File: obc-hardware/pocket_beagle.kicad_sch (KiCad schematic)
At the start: 18 parts, among them U101 PocketBeagle

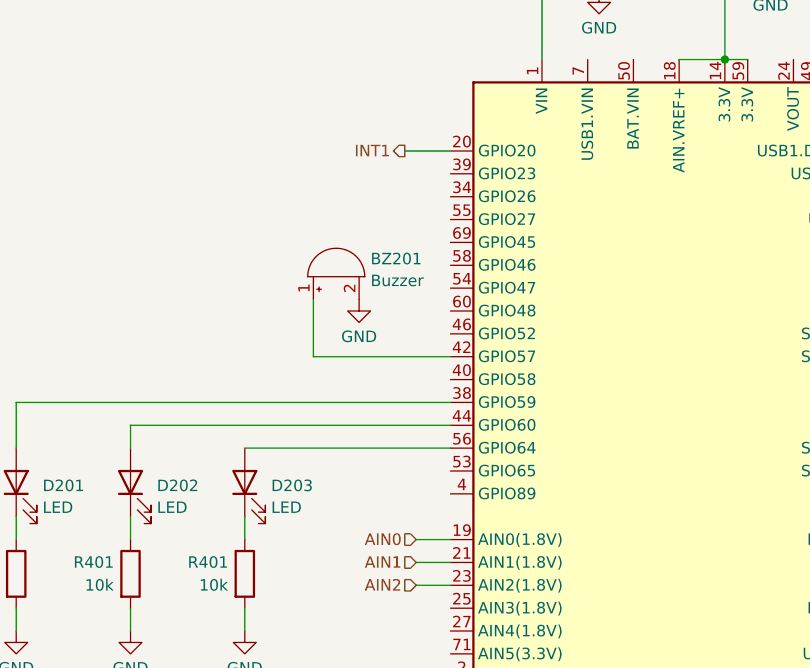
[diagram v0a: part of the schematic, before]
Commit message: added GPIO for payload
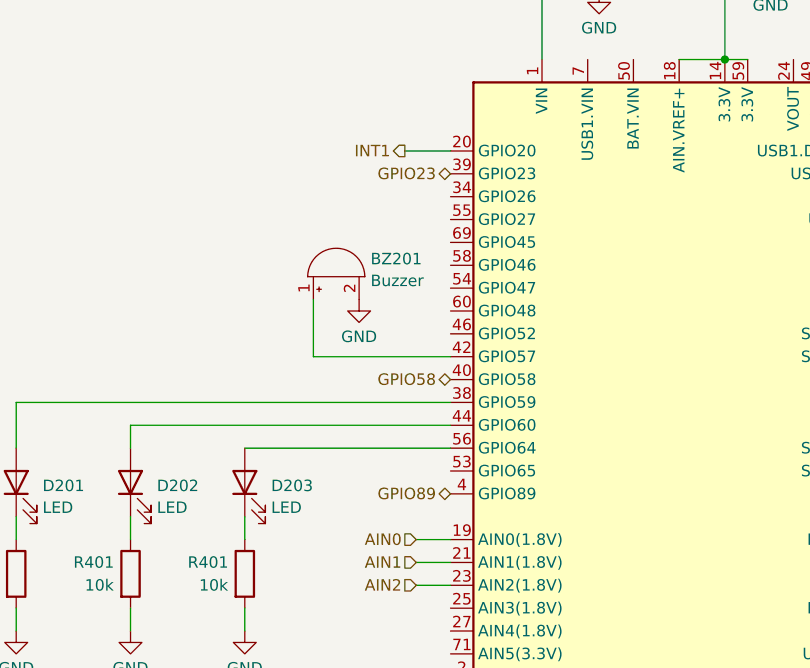
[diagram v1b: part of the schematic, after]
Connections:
- net GPIO23: now reaches U101.39 (GPIO23)
- net GPIO89: now reaches U101.4 (GPIO89)
- net GPIO58: now reaches U101.40 (GPIO58)
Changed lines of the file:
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@@
+    (effects (font (size 1.27 1.27)) (justify right))
+  )
+  (hierarchical_label "GPIO89" (shape bidirectional) (at 111.76 87.63 180) (fields_autoplaced)
+    (effects (font (size 1.27 1.27)) (justify right))
+  )
+  (hierarchical_label "GPIO58" (shape bidirectional) (at 111.76 74.93 180) (fields_autoplaced)
     (effects (font (size 1.27 1.27)) (justify right))
   )
@@
     (effects (font (size 1.27 1.27)) (justify right))
   )
+  (hierarchical_label "GPIO23" (shape bidirectional) (at 111.76 52.07 180) (fields_autoplaced)
+    (effects (font (size 1.27 1.27)) (justify right))
+  )

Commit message: added test points
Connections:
- net VOUT-24: now reaches U101.24 (VOUT)
- net AIN3: now reaches U101.25 (AIN3(1.8V))
- net AIN4: now reaches U101.27 (AIN4(1.8V))
- net PRU0.1: now reaches U101.33 (PRU0.1)
- net GPIO26: now reaches U101.34 (GPIO26)
- net PWM0A: now reaches U101.36 (PWM0A)
- net VOUT-49: now reaches U101.49 (VOUT)
- net BAT.VIN: now reaches U101.50 (BAT.VIN)
- net GPIO27: now reaches U101.55 (GPIO27)
- net PRU0.2: now reaches U101.68 (PRU0.2)
- net GPIO45: now reaches U101.69 (GPIO45)
- net AIN5: now reaches U101.71 (AIN5(3.3V))
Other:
- moved on the sheet: BZ201
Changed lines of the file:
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@@
+    (stroke (width 0) (type default))
+  )
+  (wire (pts (xy 166.37 120.65) (xy 162.56 120.65))
     (stroke (width 0) (type default))
   )
@@
     (stroke (width 0) (type default))
   )
-  (wire (pts (xy 96.52 72.39) (xy 96.52 66.04))
+  (wire (pts (xy 82.55 72.39) (xy 82.55 66.04))
     (stroke (width 0) (type default))
   )
@@
     (stroke (width 0) (type default))
   )
+  (wire (pts (xy 109.22 118.11) (xy 111.76 118.11))
+    (stroke (width 0) (type default))
+  )
   (wire (pts (xy 191.77 20.32) (xy 191.77 21.59))
     (stroke (width 0) (type default))
@@
     (stroke (width 0) (type default))
   )
+  (wire (pts (xy 149.86 36.83) (xy 149.86 39.37))
+    (stroke (width 0) (type default))
+  )
   (wire (pts (xy 76.2 100.33) (xy 76.2 102.87))
     (stroke (width 0) (type default))
@@
     (stroke (width 0) (type default))
   )
+  (wire (pts (xy 106.68 57.15) (xy 111.76 57.15))
+    (stroke (width 0) (type default))
+  )
   (wire (pts (xy 88.9 100.33) (xy 88.9 102.87))
     (stroke (width 0) (type default))
@@
     (stroke (width 0) (type default))
   )
+  (wire (pts (xy 109.22 115.57) (xy 111.76 115.57))
+    (stroke (width 0) (type default))
+  )
   (wire (pts (xy 182.88 21.59) (xy 191.77 21.59))
     (stroke (width 0) (type default))
@@
     (stroke (width 0) (type default))
   )
+  (wire (pts (xy 107.95 102.87) (xy 111.76 102.87))
+    (stroke (width 0) (type default))
+  )
+  (wire (pts (xy 106.68 52.07) (xy 111.76 52.07))
+    (stroke (width 0) (type default))
+  )
   (wire (pts (xy 107.95 97.79) (xy 111.76 97.79))
     (stroke (width 0) (type default))
@@
     (stroke (width 0) (type default))
   )
+  (wire (pts (xy 107.95 105.41) (xy 111.76 105.41))
+    (stroke (width 0) (type default))
+  )
   (wire (pts (xy 76.2 80.01) (xy 76.2 82.55))
     (stroke (width 0) (type default))
@@
     (stroke (width 0) (type default))
   )
+  (wire (pts (xy 106.68 54.61) (xy 111.76 54.61))
+    (stroke (width 0) (type default))
+  )
+  (wire (pts (xy 161.29 39.37) (xy 152.4 39.37))
+    (stroke (width 0) (type default))
+  )
   (wire (pts (xy 204.47 97.79) (xy 162.56 97.79))
     (stroke (width 0) (type default))
   )
+  (wire (pts (xy 161.29 36.83) (xy 149.86 36.83))
+    (stroke (width 0) (type default))
+  )
   (wire (pts (xy 204.47 102.87) (xy 204.47 97.79))
     (stroke (width 0) (type default))
@@
     (stroke (width 0) (type default))
   )
+  (wire (pts (xy 107.95 100.33) (xy 111.76 100.33))
+    (stroke (width 0) (type default))
+  )
   (wire (pts (xy 76.2 90.17) (xy 76.2 92.71))
     (stroke (width 0) (type default))
@@
     (stroke (width 0) (type default))
   )
+  (wire (pts (xy 106.68 59.69) (xy 111.76 59.69))
+    (stroke (width 0) (type default))
+  )
   (wire (pts (xy 203.2 105.41) (xy 203.2 100.33))
     (stroke (width 0) (type default))
   )
-  (wire (pts (xy 111.76 72.39) (xy 96.52 72.39))
+  (wire (pts (xy 111.76 72.39) (xy 82.55 72.39))
     (stroke (width 0) (type default))
   )
@@
     (effects (font (size 1.27 1.27)) (justify right))
   )
+  (hierarchical_label "VOUT-49" (shape output) (at 161.29 39.37 0) (fields_autoplaced)
+    (effects (font (size 1.27 1.27)) (justify left))
+  )
   (hierarchical_label "AIN0" (shape input) (at 107.95 92.71 180) (fields_autoplaced)
     (effects (font (size 1.27 1.27)) (justify right))
   )
+  (hierarchical_label "VOUT-24" (shape output) (at 161.29 36.83 0) (fields_autoplaced)
+    (effects (font (size 1.27 1.27)) (justify left))
+  )
+  (hierarchical_label "GPIO27" (shape bidirectional) (at 106.68 57.15 180) (fields_autoplaced)
+    (effects (font (size 1.27 1.27)) (justify right))
+  )
   (hierarchical_label "GPIO89" (shape bidirectional) (at 111.76 87.63 180) (fields_autoplaced)
     (effects (font (size 1.27 1.27)) (justify right))
   )
+  (hierarchical_label "GPIO45" (shape bidirectional) (at 106.68 59.69 180) (fields_autoplaced)
+    (effects (font (size 1.27 1.27)) (justify right))
+  )
+  (hierarchical_label "GPIO26" (shape bidirectional) (at 106.68 54.61 180) (fields_autoplaced)
+    (effects (font (size 1.27 1.27)) (justify right))
+  )
   (hierarchical_label "GPIO58" (shape bidirectional) (at 111.76 74.93 180) (fields_autoplaced)
     (effects (font (size 1.27 1.27)) (justify right))
@@
     (effects (font (size 1.27 1.27)) (justify right))
   )
-  (hierarchical_label "GPIO23" (shape bidirectional) (at 111.76 52.07 180) (fields_autoplaced)
+  (hierarchical_label "PWM0A" (shape output) (at 166.37 120.65 0) (fields_autoplaced)
+    (effects (font (size 1.27 1.27)) (justify left))
+  )
+  (hierarchical_label "BAT.VIN" (shape input) (at 132.08 39.37 90) (fields_autoplaced)
+    (effects (font (size 1.27 1.27)) (justify left))
+  )
+  (hierarchical_label "AIN5" (shape input) (at 107.95 105.41 180) (fields_autoplaced)
+    (effects (font (size 1.27 1.27)) (justify right))
+  )
+  (hierarchical_label "PRU0.2" (shape output) (at 109.22 118.11 180) (fields_autoplaced)
+    (effects (font (size 1.27 1.27)) (justify right))
+  )
+  (hierarchical_label "AIN3" (shape input) (at 107.95 100.33 180) (fields_autoplaced)
+    (effects (font (size 1.27 1.27)) (justify right))
+  )
+  (hierarchical_label "PRU0.1" (shape output) (at 109.22 115.57 180) (fields_autoplaced)
+    (effects (font (size 1.27 1.27)) (justify right))
+  )
+  (hierarchical_label "GPIO23" (shape bidirectional) (at 106.68 52.07 180) (fields_autoplaced)
+    (effects (font (size 1.27 1.27)) (justify right))
+  )
+  (hierarchical_label "AIN4" (shape input) (at 107.95 102.87 180) (fields_autoplaced)
     (effects (font (size 1.27 1.27)) (justify right))
   )
@@
     )
   )
-  (symbol (lib_id "power:GND") (at 101.6 66.04 0) (unit 1)
-    (in_bom yes) (on_board yes) (dnp no) (fields_autoplaced)
-    (property "Reference" "#PWR0216" (at 101.6 72.39 0)
-      (effects (font (size 1.27 1.27)) hide)
-    )
-    (property "Value" "GND" (at 101.6 70.1731 0)
-      (effects (font (size 1.27 1.27)))
-    )
-    (property "Footprint" "" (at 101.6 66.04 0)
-      (effects (font (size 1.27 1.27)) hide)
-    )
-    (property "Datasheet" "" (at 101.6 66.04 0)
+  (symbol (lib_id "power:GND") (at 87.63 66.04 0) (unit 1)
+    (in_bom yes) (on_board yes) (dnp no) (fields_autoplaced)
+    (property "Reference" "#PWR0216" (at 87.63 72.39 0)
+      (effects (font (size 1.27 1.27)) hide)
+    )
+    (property "Value" "GND" (at 87.63 70.1731 0)
+      (effects (font (size 1.27 1.27)))
+    )
+    (property "Footprint" "" (at 87.63 66.04 0)
+      (effects (font (size 1.27 1.27)) hide)
+    )
+    (property "Datasheet" "" (at 87.63 66.04 0)
       (effects (font (size 1.27 1.27)) hide)
     )
@@
     )
   )
-  (symbol (lib_id "Device:Buzzer") (at 99.06 63.5 90) (unit 1)
-    (in_bom yes) (on_board yes) (dnp no) (fields_autoplaced)
-    (property "Reference" "BZ201" (at 102.87 61.5328 90)
+  (symbol (lib_id "Device:Buzzer") (at 85.09 63.5 90) (unit 1)
+    (in_bom yes) (on_board yes) (dnp no) (fields_autoplaced)
+    (property "Reference" "BZ201" (at 88.9 61.5328 90)
       (effects (font (size 1.27 1.27)) (justify right))
     )
-    (property "Value" "Buzzer" (at 102.87 63.957 90)
+    (property "Value" "Buzzer" (at 88.9 63.957 90)
       (effects (font (size 1.27 1.27)) (justify right))
     )
-    (property "Footprint" "Buzzer_Beeper:Buzzer_12x9.5RM7.6" (at 96.52 64.135 90)
-      (effects (font (size 1.27 1.27)) hide)
-    )
-    (property "Datasheet" "~" (at 96.52 64.135 90)
-      (effects (font (size 1.27 1.27)) hide)
-    )
+    (property "Footprint" "Buzzer_Beeper:Buzzer_12x9.5RM7.6" (at 82.55 64.135 90)
+      (effects (font (size 1.27 1.27)) hide)
+    )
+    (property "Datasheet" "~" (at 82.55 64.135 90)
+      (effects (font (size 1.27 1.27)) hide)
+    )
